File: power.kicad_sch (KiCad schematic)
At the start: 45 parts, among them J2 BATT_CON, J3 PWR_HDR, U10 NCP164CSN330T1G, U2 BQ25622, U5 TPS22995RZFR, U6 MIC2876-5.25YMT-TR

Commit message: v1.14 mods
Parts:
- J2: footprint Connector_JST:JST_XH_B3B-XH-A_1x03_P2.50mm_Vertical -> effectiveRangeHat:CONN03_533750310_MOL
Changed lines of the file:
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@@
 	(label "SYSLOAD"
 		(at 243.84 102.87 0)
-		(fields_autoplaced yes)
 		(effects
 			(font
@@
 	(label "REGN"
 		(at 97.79 66.04 0)
-		(fields_autoplaced yes)
 		(effects
 			(font
@@
 	(label "SYS5V"
 		(at 78.74 161.29 0)
-		(fields_autoplaced yes)
 		(effects
 			(font
@@
 	(label "STAT_LED"
 		(at 78.74 177.8 0)
-		(fields_autoplaced yes)
 		(effects
 			(font
@@
 	(label "TS_BIAS"
 		(at 101.6 76.2 0)
-		(fields_autoplaced yes)
 		(effects
 			(font
@@
 	(label "ILIM"
 		(at 66.04 66.04 0)
-		(fields_autoplaced yes)
 		(effects
 			(font
@@
 	(label "TS_BYPASS"
 		(at 107.95 168.91 180)
-		(fields_autoplaced yes)
 		(effects
 			(font
@@
 	(label "~{PG}_LED"
 		(at 66.04 177.8 0)
-		(fields_autoplaced yes)
 		(effects
 			(font
@@
 	(label "L2"
 		(at 194.31 35.56 0)
-		(fields_autoplaced yes)
 		(effects
 			(font
@@
 	(label "BTST"
 		(at 104.14 62.23 0)
-		(fields_autoplaced yes)
 		(effects
 			(font
@@
 	(label "BAT"
 		(at 101.6 73.66 0)
-		(fields_autoplaced yes)
 		(effects
 			(font
@@
 	(label "SYS5V"
 		(at 119.38 100.33 0)
-		(fields_autoplaced yes)
 		(effects
 			(font
@@
 	(label "VREF"
 		(at 26.67 80.01 0)
-		(fields_autoplaced yes)
 		(effects
 			(font
@@
 	(label "LDO_PG"
 		(at 245.11 96.52 0)
-		(fields_autoplaced yes)
 		(effects
 			(font
@@
 	(label "SYS5V"
 		(at 167.64 133.35 180)
-		(fields_autoplaced yes)
 		(effects
 			(font
@@
 	(label "BQ_VBUS"
 		(at 66.04 60.96 0)
-		(fields_autoplaced yes)
 		(effects
 			(font
@@
 	(label "PWR_LED_CAT"
 		(at 115.57 109.22 0)
-		(fields_autoplaced yes)
 		(effects
 			(font
@@
 	(label "STAT"
 		(at 78.74 189.23 0)
-		(fields_autoplaced yes)
 		(effects
 			(font
@@
 	(label "SYSLOAD"
 		(at 134.62 49.53 0)
-		(fields_autoplaced yes)
 		(effects
 			(font
@@
 	(label "TS"
 		(at 127 168.91 0)
-		(fields_autoplaced yes)
 		(effects
 			(font
@@
 	(label "~{QON}"
 		(at 101.6 95.25 0)
-		(fields_autoplaced yes)
 		(effects
 			(font
@@
 	(label "BQ_VBUS"
 		(at 100.33 22.86 0)
-		(fields_autoplaced yes)
 		(effects
 			(font
@@
 	(label "SYSLOAD"
 		(at 101.6 71.12 0)
-		(fields_autoplaced yes)
 		(effects
 			(font
@@
 	(label "PMID"
 		(at 36.83 165.1 0)
-		(fields_autoplaced yes)
 		(effects
 			(font
@@
 	(label "SYSLOAD"
 		(at 234.95 38.1 0)
-		(fields_autoplaced yes)
 		(effects
 			(font
@@
 	(label "~{PG}"
 		(at 66.04 189.23 0)
-		(fields_autoplaced yes)
 		(effects
 			(font
@@
 	(label "TS"
 		(at 101.6 78.74 0)
-		(fields_autoplaced yes)
 		(effects
 			(font
@@
 	(label "5VEN"
 		(at 196.85 55.88 0)
-		(fields_autoplaced yes)
 		(effects
 			(font
@@
 	(label "STAT"
 		(at 66.04 68.58 0)
-		(fields_autoplaced yes)
 		(effects
 			(font
@@
 	(label "TS_BIAS"
 		(at 133.35 158.75 0)
-		(fields_autoplaced yes)
 		(effects
 			(font
@@
 	(label "ILIM"
 		(at 22.86 165.1 0)
-		(fields_autoplaced yes)
 		(effects
 			(font
@@
 	(label "VREF"
 		(at 46.99 64.77 0)
-		(fields_autoplaced yes)
 		(effects
 			(font
@@
 	(label "5VPG"
 		(at 234.95 53.34 180)
-		(fields_autoplaced yes)
 		(effects
 			(font
@@
 	(label "SYSLOAD"
 		(at 201.93 93.98 180)
-		(fields_autoplaced yes)
 		(effects
 			(font
@@
 	(label "SW"
 		(at 99.06 48.26 0)
-		(fields_autoplaced yes)
 		(effects
 			(font
@@
 	(label "VBUS"
 		(at 80.01 22.86 0)
-		(fields_autoplaced yes)
 		(effects
 			(font
@@
 	(label "VREF"
 		(at 57.15 64.77 0)
-		(fields_autoplaced yes)
 		(effects
 			(font
@@
 	(label "BAT"
 		(at 48.26 110.49 0)
-		(fields_autoplaced yes)
 		(effects
 			(font
@@
 	(label "SYS5V"
 		(at 257.81 49.53 0)
-		(fields_autoplaced yes)
 		(effects
 			(font
@@
 	(label "5VLED"
 		(at 269.24 64.77 180)
-		(fields_autoplaced yes)
 		(effects
 			(font
@@
 	(label "~{PG}"
 		(at 66.04 71.12 0)
-		(fields_autoplaced yes)
 		(effects
 			(font
@@
 	(label "SYS5V"
 		(at 66.04 161.29 0)
-		(fields_autoplaced yes)
 		(effects
 			(font
@@
 	(label "PMID"
 		(at 66.04 63.5 0)
-		(fields_autoplaced yes)
 		(effects
 			(font
@@
 	(label "TS"
 		(at 45.72 120.65 180)
-		(fields_autoplaced yes)
 		(effects
 			(font
@@
 		(shape output)
 		(at 125.73 95.25 0)
-		(fields_autoplaced yes)
 		(effects
 			(font
@@
 		(shape input)
 		(at 180.34 148.59 0)
-		(fields_autoplaced yes)
 		(effects
 			(font
@@
 		(shape input)
 		(at 116.84 119.38 0)
-		(fields_autoplaced yes)
 		(effects
 			(font
@@
 		(shape bidirectional)
 		(at 67.31 73.66 180)
-		(fields_autoplaced yes)
 		(effects
 			(font
@@
 		(shape output)
 		(at 40.64 78.74 180)
-		(fields_autoplaced yes)
 		(effects
 			(font
@@
 		(shape input)
 		(at 67.31 83.82 180)
-		(fields_autoplaced yes)
 		(effects
 			(font
@@
 		(shape input)
 		(at 24.13 80.01 180)
-		(fields_autoplaced yes)
 		(effects
 			(font
@@
 		(shape output)
 		(at 220.98 135.89 0)
-		(fields_autoplaced yes)
 		(effects
 			(font
@@
 		(shape output)
 		(at 118.11 22.86 0)
-		(fields_autoplaced yes)
 		(effects
 			(font
@@
 		(shape input)
 		(at 36.83 22.86 180)
-		(fields_autoplaced yes)
 		(effects
 			(font
@@
 		(shape output)
 		(at 269.24 46.99 0)
-		(fields_autoplaced yes)
 		(effects
 			(font
@@
 		(shape input)
 		(at 67.31 76.2 180)
-		(fields_autoplaced yes)
 		(effects
 			(font
@@
 		(shape output)
 		(at 44.45 114.3 180)
-		(fields_autoplaced yes)
 		(effects
 			(font
@@
 			)
 		)
-		(property "Footprint" "Connector_JST:JST_XH_B3B-XH-A_1x03_P2.50mm_Vertical"
+		(property "Footprint" "effectiveRangeHat:CONN03_533750310_MOL"
 			(at 45.72 128.27 0)
 			(effects

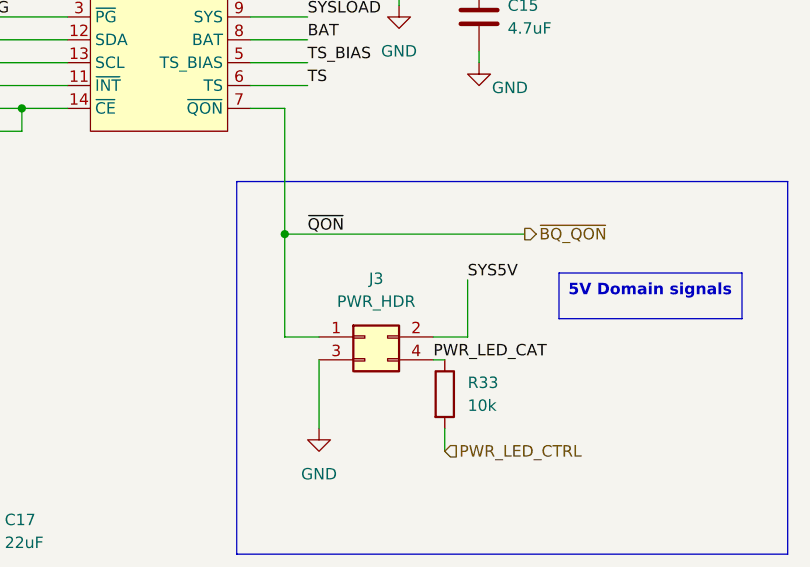
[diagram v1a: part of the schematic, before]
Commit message: connector reorg, trace adjustments
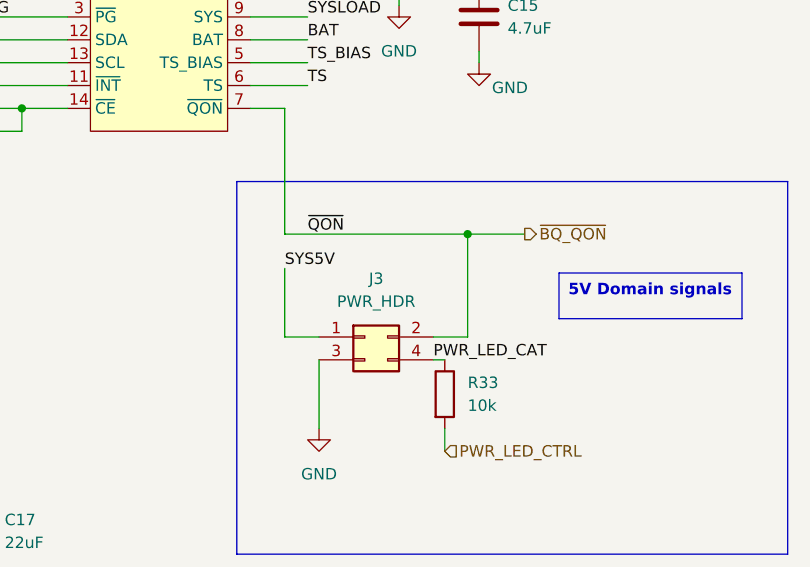
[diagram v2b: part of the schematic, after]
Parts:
- J2: MPN B3B-XH-A -> 533750310; Manufacturer JST Sales America Inc. -> Molex; SupplierLink (none) -> https://eu.mouser.com/ProductDetail/Molex/53375-0310?qs=kD7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
- J3: footprint Connector_PinHeader_2.54mm:PinHeader_2x02_P2.54mm_Vertical -> Connector_PinHeader_2.00mm:PinHeader_2x02_P2.00mm_Vertical; MPN 61300421121 -> DF11-4DP-2DSA(08); Manufacturer Würth Elektronik -> Hirose Electric Co Ltd; SupplierLink https://www.digikey.hu/en/products/detail/w%C3%BCrth-elektr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 -> https://eu.mouser.com/ProductDetail/Hirose-Connector/DF11-4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
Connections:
- net SYS5V: now also J3.1 (Pin_1); no longer J3.2 (Pin_2)
- net ~{BQ_QON}: now also J3.2 (Pin_2); no longer J3.1 (Pin_1)
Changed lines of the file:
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@@
 	)
 	(junction
-		(at 99.06 95.25)
+		(at 256.54 93.98)
 		(diameter 0)
 		(color 0 0 0 0)
 	)
 	(junction
-		(at 256.54 93.98)
+		(at 180.34 133.35)
 		(diameter 0)
 		(color 0 0 0 0)
 	)
 	(junction
-		(at 180.34 133.35)
+		(at 199.39 104.14)
 		(diameter 0)
 		(color 0 0 0 0)
 	)
 	(junction
-		(at 199.39 104.14)
+		(at 119.38 95.25)
 		(diameter 0)
 		(color 0 0 0 0)
@@
 	(wire
 		(pts
-			(xy 99.06 95.25) (xy 99.06 106.68)
-		)
-		(stroke
-			(width 0)
-			(type default)
-		)
-	)
-	(wire
-		(pts
 			(xy 231.14 138.43) (xy 231.14 152.4)
 		)
@@
 	(wire
 		(pts
-			(xy 119.38 100.33) (xy 119.38 106.68)
-		)
-		(stroke
-			(width 0)
-			(type default)
-		)
-	)
-	(wire
-		(pts
 			(xy 64.77 121.92) (xy 64.77 124.46)
 		)
@@
 	(wire
 		(pts
+			(xy 99.06 106.68) (xy 99.06 99.06)
+		)
+		(stroke
+			(width 0)
+			(type default)
+		)
+	)
+	(wire
+		(pts
 			(xy 44.45 114.3) (xy 48.26 114.3)
 		)
@@
 	(wire
 		(pts
-			(xy 99.06 95.25) (xy 125.73 95.25)
+			(xy 99.06 95.25) (xy 119.38 95.25)
 		)
 		(stroke
@@
 	(wire
 		(pts
+			(xy 119.38 95.25) (xy 119.38 106.68)
+		)
+		(stroke
+			(width 0)
+			(type default)
+		)
+	)
+	(wire
+		(pts
 			(xy 95.25 81.28) (xy 99.06 81.28)
 		)
@@
 		)
 	)
+	(wire
+		(pts
+			(xy 119.38 95.25) (xy 125.73 95.25)
+		)
+		(stroke
+			(width 0)
+			(type default)
+		)
+	)
 	(rectangle
 		(start 13.716 12.446)
@@
 	)
 	(label "SYS5V"
-		(at 119.38 100.33 0)
+		(at 99.06 99.06 0)
 		(effects
 			(font
@@
 			)
 		)
-		(property "Footprint" "Connector_PinHeader_2.54mm:PinHeader_2x02_P2.54mm_Vertical"
+		(property "Footprint" "Connector_PinHeader_2.00mm:PinHeader_2x02_P2.00mm_Vertical"
 			(at 107.95 106.68 0)
 			(effects
@@
 			)
 		)
-		(property "MPN" "61300421121"
+		(property "MPN" "DF11-4DP-2DSA(08)"
 			(at 107.95 106.68 0)
 			(effects
@@
 			)
 		)
-		(property "Manufacturer" "Würth Elektronik"
+		(property "Manufacturer" "Hirose Electric Co Ltd"
 			(at 107.95 106.68 0)
 			(effects
@@
 			)
 		)
-		(property "SupplierLink" "https://www.digikey.hu/en/products/detail/w%C3%BCrth-elektronik/61300421121/4846829"
+		(property "SupplierLink" "https://eu.mouser.com/ProductDetail/Hirose-Connector/DF11-4DP-2DSA08?qs=Ux3WWAnHpjDPTWEXT%2FLWvg%3D%3D&utm_id=6470817810&utm_source=google&utm_medium=cpc&utm_marketing_tactic=emeacorp&gad_source=1&gclid=Cj0KCQiA_Yq-BhC9ARIsAA6fbAgTsAei4DpP3br8qNNzYN_Dkzz6xPuYT9pN7YQk0zNSuUX4IH3RYHEaAunPEALw_wcB"
 			(at 107.95 106.68 0)
 			(effects
@@
 			)
 		)
-		(property "MPN" "B3B-XH-A"
+		(property "MPN" "533750310"
 			(at 45.72 128.27 0)
 			(effects
@@
 			)
 		)
-		(property "Manufacturer" "JST Sales America Inc."
+		(property "Manufacturer" "Molex"
 			(at 45.72 128.27 0)
 			(effects
 				(font
+					(size 1.27 1.27)
+				)
+				(hide yes)
+			)
+		)
+		(property "SupplierLink" "https://eu.mouser.com/ProductDetail/Molex/53375-0310?qs=kD7lmHUVEJbTZwckk9uvMw%3D%3D&utm_source=OEMSecrets&utm_medium=aggregator&utm_campaign=533750310&utm_term=533750310&utm_content=Molex&_gl=1*a7gvlm*_ga*dW5kZWZpbmVk*_ga_15W4STQT4T*dW5kZWZpbmVk*_ga_1KQLCYKRX3*dW5kZWZpbmVk"
+			(at 45.72 128.27 90)
+			(effects
+				(font
